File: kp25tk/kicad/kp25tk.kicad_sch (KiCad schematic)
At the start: 53 parts, among them J1 Host Connector, J2 Config Header, J3 Power In, J4 Row Select In, J5 Column Out, J6 NMI Out, J7 Reset Out, J8 Switch, SW0 KEY00, SW1 KEY01, SW10 KEY0A, SW11 KEY0B, SW12 KEY0C, SW13 KEY0D, SW14 KEY0E, SW15 KEY0F, SW16 KEY10, SW17 KEY11, SW18 KEY12, SW19 KEY13, SW2 KEY02, SW20 KEY14, SW21 KEY15, SW22 KEY16, SW23 KEY17, SW24 NMI, SW25 RESET, SW27 SWITCH, SW3 KEY03, SW4 KEY04, SW5 KEY05, SW6 KEY06, SW7 KEY07, SW8 KEY08, SW9 KEY09, U1 74LS14

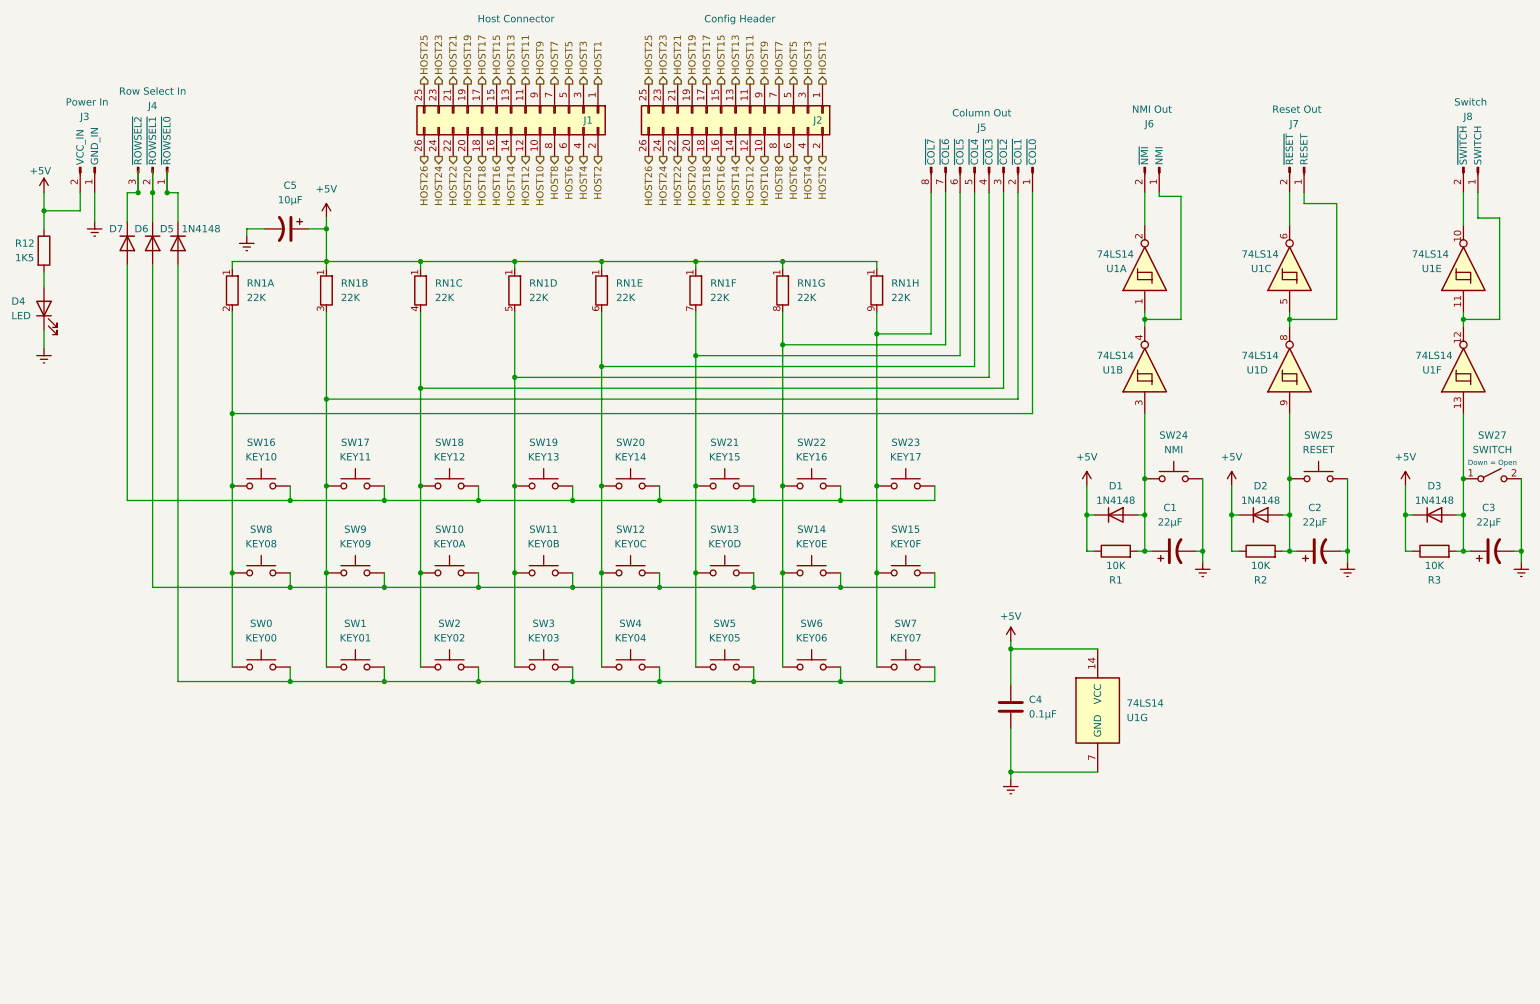
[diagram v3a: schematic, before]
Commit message: kp25tk/: v0.0.5 Schottky diodes, diodes in matrix
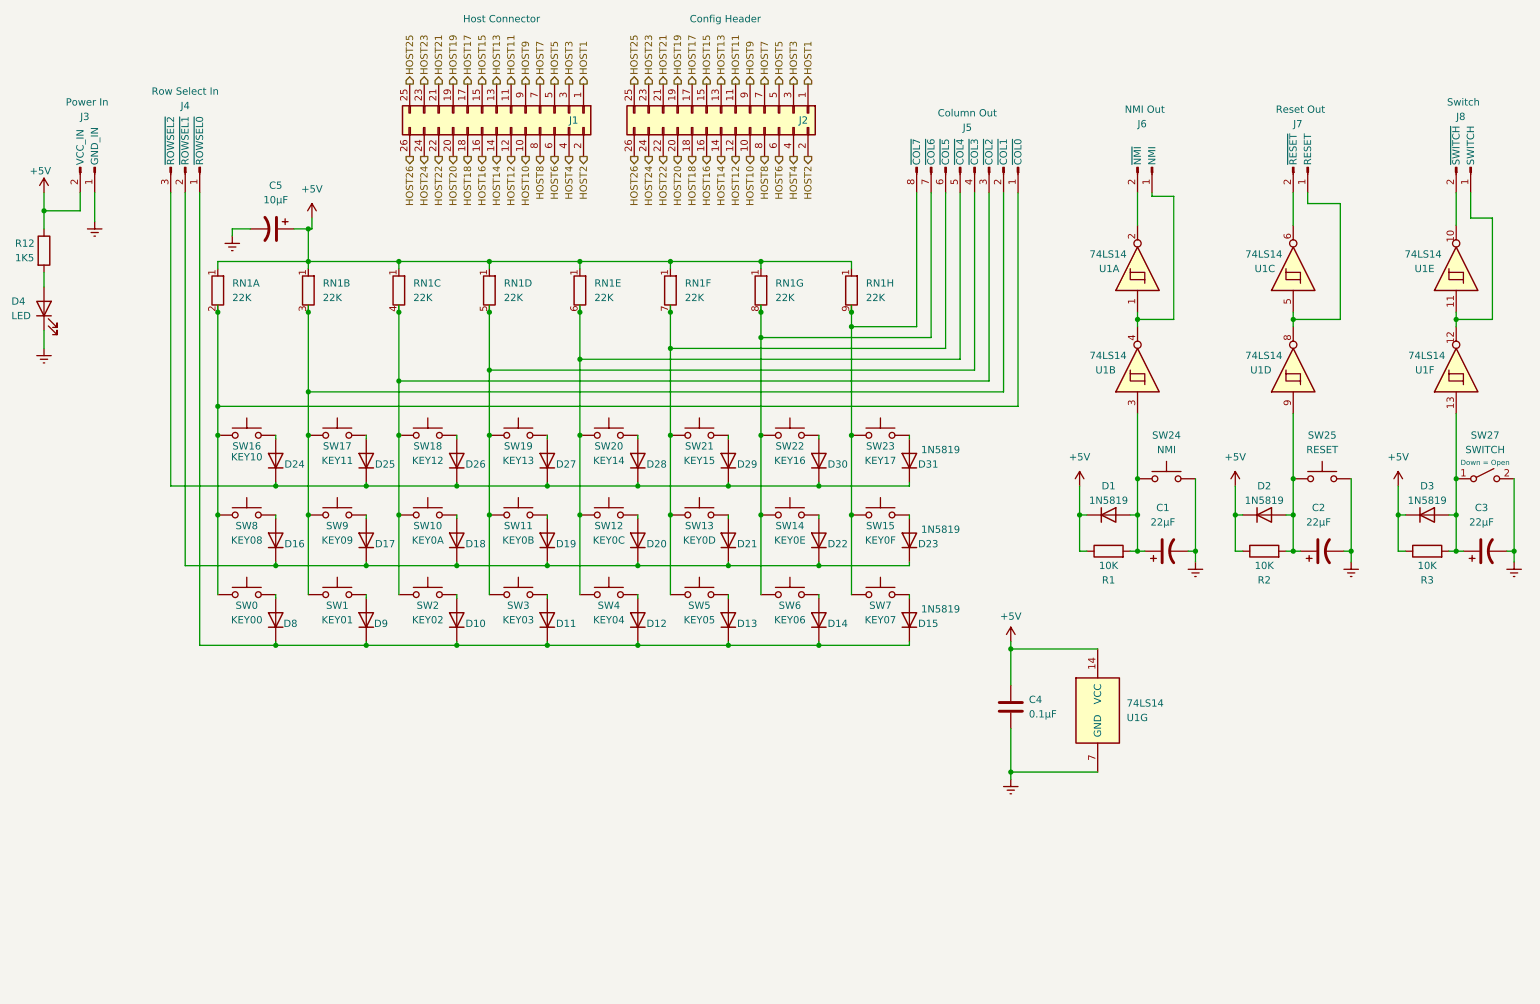
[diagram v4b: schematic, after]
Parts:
- removed D5, D6, D7: 1N4148, Diode_THT:D_DO-35_SOD27_P7.62mm_Horizontal, symbol Diode:1N4148
- added D10, D11, D12, D13, D14, D15, D16, D17, D18, D19, D20, D21, D22, D23, D24, D25, D26, D27, D28, D29, D30, D31, D8, D9: 1N5819, Diode_THT:D_DO-35_SOD27_P7.62mm_Horizontal, symbol Diode:1N4148
- D1, D2, D3: value 1N4148 -> 1N5819
- SW0, SW1, SW10, SW11, SW12, SW13, SW14, SW15, SW16, SW17, SW18, SW19, SW2, SW20, SW21, SW22, SW23, SW24, SW3, SW4, SW5, SW6, SW7, SW8, SW9: footprint Button_Switch_Keyboard:SW_Cherry_MX_1.00u_Plate -> Button_Switch_Keyboard:SW_Cherry_MX_1.00u_PCB
- SW27: footprint Button_Switch_THT:SW_Slide_1P2T_CK_OS102011MS2Q -> Button_Switch_THT_Extras:SW_MINI-SPDT-SW
- U1: footprint Package_DIP:DIP-14_W7.62mm_Socket -> Package_DIP:DIP-14_W7.62mm
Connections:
- net at J4.1 (~{ROWSEL0}): now also D10.1 (K), D11.1 (K), D12.1 (K), D13.1 (K), D14.1 (K), D15.1 (K), D8.1 (K), D9.1 (K)
- net at J4.2 (~{ROWSEL1}): now also D16.1 (K), D17.1 (K), D18.1 (K), D19.1 (K), D20.1 (K), D21.1 (K), D22.1 (K), D23.1 (K)
- net at J4.3 (~{ROWSEL2}): now also D24.1 (K), D25.1 (K), D26.1 (K), D27.1 (K), D28.1 (K), D29.1 (K), D30.1 (K), D31.1 (K)
- new net: D25.2 (A), SW17.2
- new net: D8.2 (A), SW0.2
- new net: D16.2 (A), SW8.2
- new net: D24.2 (A), SW16.2
- new net: D21.2 (A), SW13.2
- new net: D23.2 (A), SW15.2
- new net: D20.2 (A), SW12.2
- new net: D14.2 (A), SW6.2
- new net: D12.2 (A), SW4.2
- new net: D22.2 (A), SW14.2
- new net: D31.2 (A), SW23.2
- new net: D26.2 (A), SW18.2
- new net: D30.2 (A), SW22.2
- new net: D18.2 (A), SW10.2
- new net: D29.2 (A), SW21.2
- new net: D17.2 (A), SW9.2
- new net: D9.2 (A), SW1.2
- new net: D19.2 (A), SW11.2
- new net: D11.2 (A), SW3.2
- new net: D28.2 (A), SW20.2
- new net: D27.2 (A), SW19.2
- new net: D15.2 (A), SW7.2
- new net: D10.2 (A), SW2.2
- new net: D13.2 (A), SW5.2
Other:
- moved on the sheet: C1, C2, C3, C5, D1, D2, D3, J1, J2, J4, J5, J6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

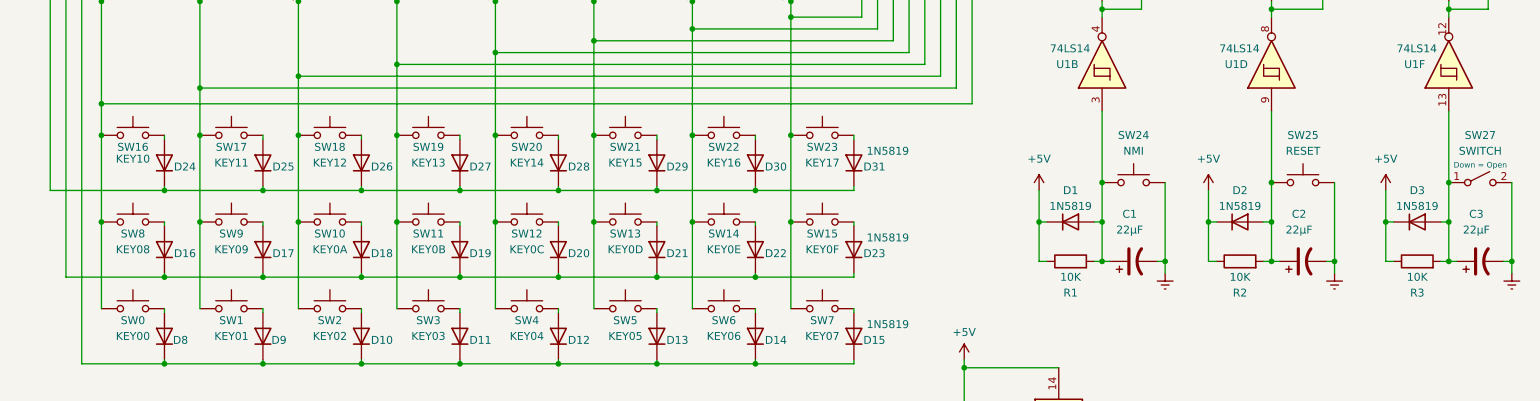
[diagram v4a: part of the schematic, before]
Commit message: kp25tk/: v0.0.6 SPDT switch, improve PCB component locations/labels
We still need to go through and fix all the keyswitch labels to be
just the key name, without the SWnn.
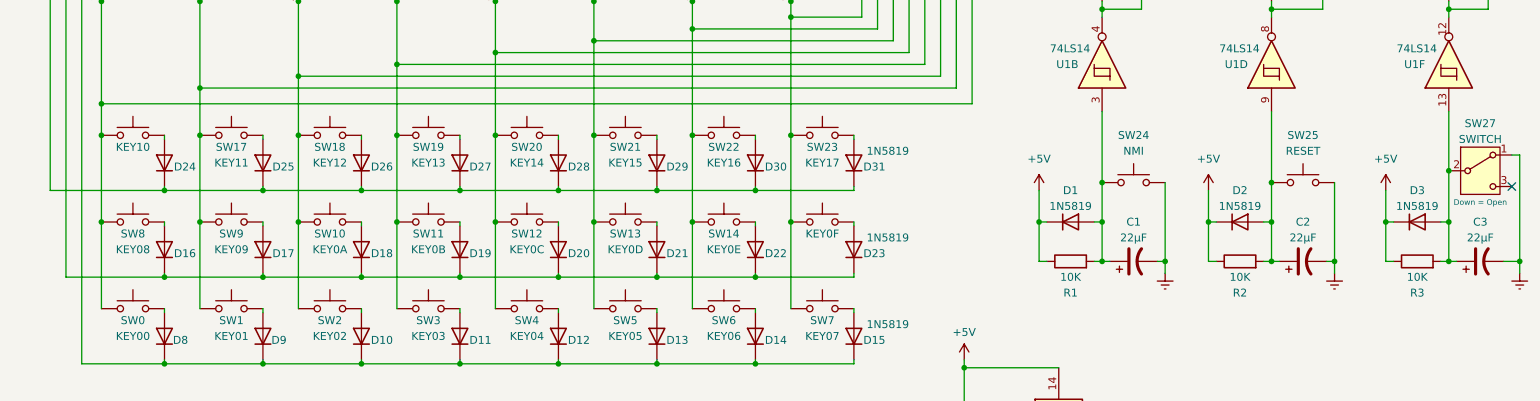
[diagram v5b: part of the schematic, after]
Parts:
- SW27: symbol Switch:SW_SPST -> Switch:SW_SPDT
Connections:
- net Earth: now also SW27.1 (A); no longer SW27.2 (B)
- net at C3.1, D3.2 (A), R3.2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: now also SW27.2 (B); no longer SW27.1 (A)
- no-connect marks 0 -> 1
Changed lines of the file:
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@@
   (title_block
     (title "KP25TK 25 Key Hex Keyboard")
-    (rev "0.0.5")
+    (rev "0.0.6")
     (comment 1 "Desginer: cjs")
     (comment 2 "Drafter: Andy Diags")
@@
   (junction (at 69.215 85.725) (diameter 0) (color 0 0 0 0)
   )
-  (junction (at 280.67 113.665) (diameter 0) (color 0 0 0 0)
+  (junction (at 281.94 113.665) (diameter 0) (color 0 0 0 0)
   )
   (junction (at 95.25 130.175) (diameter 0) (color 0 0 0 0)
@@
   (junction (at 241.935 100.965) (diameter 0) (color 0 0 0 0)
   )
+  (junction (at 270.51 99.06) (diameter 0) (color 0 0 0 0)
+  )
   (junction (at 148.59 107.315) (diameter 0) (color 0 0 0 0)
   )
@@
   (junction (at 100.965 81.915) (diameter 0) (color 0 0 0 0)
   )
-  (junction (at 270.51 100.965) (diameter 0) (color 0 0 0 0)
-  )
   (junction (at 53.34 71.755) (diameter 0) (color 0 0 0 0)
   )
@@
   (junction (at 85.09 83.82) (diameter 0) (color 0 0 0 0)
   )
+  (no_connect (at 280.67 101.6))
   (wire (pts (xy 175.895 50.8) (xy 175.895 74.295))
     (stroke (width 0) (type default))
@@
     (stroke (width 0) (type default))
   )
+  (wire (pts (xy 280.67 96.52) (xy 281.94 96.52))
+    (stroke (width 0) (type default))
+  )
   (wire (pts (xy 85.09 62.865) (xy 100.965 62.865))
     (stroke (width 0) (type default))
@@
     (stroke (width 0) (type default))
   )
+  (wire (pts (xy 270.51 99.06) (xy 270.51 107.315))
+    (stroke (width 0) (type default))
+  )
   (wire (pts (xy 116.84 62.865) (xy 116.84 64.135))
     (stroke (width 0) (type default))
@@
     (stroke (width 0) (type default))
   )
-  (wire (pts (xy 280.67 100.965) (xy 280.67 113.665))
+  (wire (pts (xy 281.94 96.52) (xy 281.94 113.665))
     (stroke (width 0) (type default))
   )
@@
     (stroke (width 0) (type default))
   )
-  (wire (pts (xy 280.67 113.665) (xy 280.67 115.57))
+  (wire (pts (xy 281.94 113.665) (xy 281.94 115.57))
     (stroke (width 0) (type default))
   )
@@
     (stroke (width 0) (type default))
   )
-  (wire (pts (xy 270.51 100.965) (xy 270.51 107.315))
-    (stroke (width 0) (type default))
-  )
   (wire (pts (xy 79.375 93.345) (xy 79.375 93.98))
     (stroke (width 0) (type default))
@@
     (stroke (width 0) (type default))
   )
-  (wire (pts (xy 279.4 113.665) (xy 280.67 113.665))
+  (wire (pts (xy 279.4 113.665) (xy 281.94 113.665))
     (stroke (width 0) (type default))
   )
@@
     (stroke (width 0) (type default))
   )
-  (wire (pts (xy 270.51 89.535) (xy 270.51 100.965))
+  (wire (pts (xy 270.51 89.535) (xy 270.51 99.06))
     (stroke (width 0) (type default))
   )
@@
     (in_bom yes) (on_board yes) (dnp no)
     (property "Reference" "SW15" (at 169.545 109.22 0)
-      (effects (font (size 1.27 1.27)))
+      (effects (font (size 1.27 1.27)) hide)
     )
-    (property "Value" "KEY0F" (at 169.545 111.76 0)
+    (property "Value" "KEY0F" (at 169.545 109.22 0)
       (effects (font (size 1.27 1.27)))
     )
@@
     (in_bom yes) (on_board yes) (dnp no)
     (property "Reference" "SW16" (at 58.42 95.25 0)
-      (effects (font (size 1.27 1.27)))
+      (effects (font (size 1.27 1.27)) hide)
     )
-    (property "Value" "KEY10" (at 58.42 97.155 0)
+    (property "Value" "KEY10" (at 58.42 95.25 0)
       (effects (font (size 1.27 1.27)))
     )
@@
   )
   (symbol (lib_id "Device:C_Polarized_US") (at 247.015 113.665 90) (unit 1)
-    (in_bom yes) (on_board yes) (dnp no) (fields_autoplaced)
-    (property "Reference" "C2" (at 246.38 106.045 90)
+    (in_bom yes) (on_board yes) (dnp no)
+    (property "Reference" "C2" (at 247.015 107.315 90)
       (effects (font (size 1.27 1.27)))
     )
-    (property "Value" "22µF" (at 246.38 108.585 90)
+    (property "Value" "22µF" (at 247.015 109.855 90)
       (effects (font (size 1.27 1.27)))
     )
@@
     )
   )
-  (symbol (lib_id "power:Earth") (at 280.67 115.57 0) (unit 1)
+  (symbol (lib_id "power:Earth") (at 281.94 115.57 0) (unit 1)
     (in_bom yes) (on_board yes) (dnp no) (fields_autoplaced)
-    (property "Reference" "#PWR011" (at 280.67 121.92 0)
+    (property "Reference" "#PWR011" (at 281.94 121.92 0)
       (effects (font (size 1.27 1.27)) hide)
     )
-    (property "Value" "Earth" (at 280.67 119.38 0)
+    (property "Value" "Earth" (at 281.94 119.38 0)
       (effects (font (size 1.27 1.27)) hide)
     )
-    (property "Footprint" "" (at 280.67 115.57 0)
+    (property "Footprint" "" (at 281.94 115.57 0)
       (effects (font (size 1.27 1.27)) hide)
     )
-    (property "Datasheet" "~" (at 280.67 115.57 0)
+    (property "Datasheet" "~" (at 281.94 115.57 0)
       (effects (font (size 1.27 1.27)) hide)
     )
@@
     )
   )
-  (symbol (lib_id "Switch:SW_SPST") (at 275.59 100.965 0) (unit 1)
+  (symbol (lib_id "Switch:SW_SPDT") (at 275.59 99.06 0) (unit 1)
     (in_bom yes) (on_board yes) (dnp no)
-    (property "Reference" "SW27" (at 275.59 93.345 0)
+    (property "Reference" "SW27" (at 275.59 91.44 0)
       (effects (font (size 1.27 1.27)))
     )
-    (property "Value" "SWITCH" (at 275.59 95.885 0)
+    (property "Value" "SWITCH" (at 275.59 93.98 0)
       (effects (font (size 1.27 1.27)))
     )
-    (property "Footprint" "Button_Switch_THT_Extras:SW_MINI-SPDT-SW" (at 275.59 100.965 0)
+    (property "Footprint" "Button_Switch_THT_Extras:SW_MINI-SPDT-SW" (at 275.59 99.06 0)
       (effects (font (size 1.27 1.27)) hide)
     )
-    (property "Datasheet" "~" (at 275.59 100.965 0)
+    (property "Datasheet" "~" (at 275.59 106.68 0)
       (effects (font (size 1.27 1.27)) hide)
     )
-    (property "Label" "Down = Open" (at 275.59 98.125 0)
+    (property "Label" "Down = Open" (at 275.59 104.14 0)
       (effects (font (size 0.9 0.9)))
     )
     (pin "1")
     (pin "2")
+    (pin "3")
     (instances
       (project "kp25tk"
@@
   )
   (symbol (lib_id "Device:C_Polarized_US") (at 275.59 113.665 90) (unit 1)
-    (in_bom yes) (on_board yes) (dnp no) (fields_autoplaced)
-    (property "Reference" "C3" (at 274.955 106.045 90)
+    (in_bom yes) (on_board yes) (dnp no)
+    (property "Reference" "C3" (at 275.59 107.315 90)
       (effects (font (size 1.27 1.27)))
     )
-    (property "Value" "22µF" (at 274.955 108.585 90)
+    (property "Value" "22µF" (at 275.59 109.855 90)
       (effects (font (size 1.27 1.27)))
     )
@@
   )
   (symbol (lib_id "Device:C_Polarized_US") (at 219.71 113.665 90) (unit 1)
-    (in_bom yes) (on_board yes) (dnp no) (fields_autoplaced)
-    (property "Reference" "C1" (at 219.075 106.045 90)
+    (in_bom yes) (on_board yes) (dnp no)
+    (property "Reference" "C1" (at 219.71 107.315 90)
       (effects (font (size 1.27 1.27)))
     )
-    (property "Value" "22µF" (at 219.075 108.585 90)
+    (property "Value" "22µF" (at 219.71 109.855 90)
       (effects (font (size 1.27 1.27)))
     )
